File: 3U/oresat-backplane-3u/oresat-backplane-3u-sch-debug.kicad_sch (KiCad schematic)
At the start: 1 part, among them J1 m55-6001642

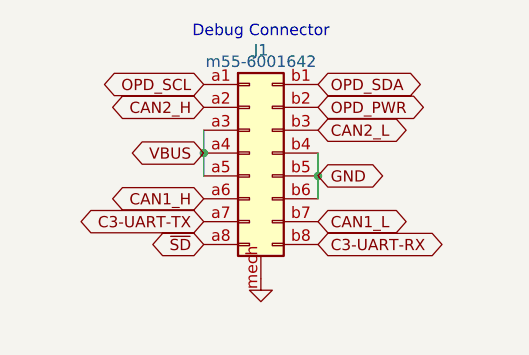
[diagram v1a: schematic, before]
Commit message: Can lines on back - need to move can resistors to front & add b.side solder mask
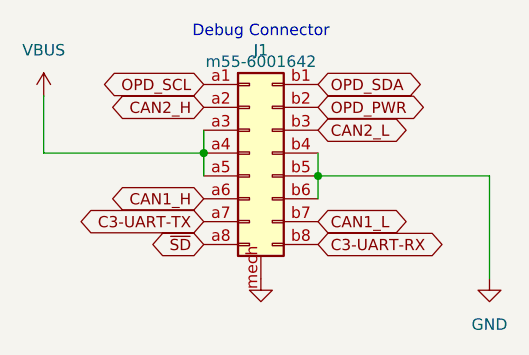
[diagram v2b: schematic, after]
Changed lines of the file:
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@@
+	(wire
+		(pts
+			(xy 167.64 114.3) (xy 167.64 120.65)
+		)
+		(stroke
+			(width 0)
+			(type default)
+		)
+	)
 	(wire
 		(pts
@@
 	(wire
 		(pts
+			(xy 217.17 123.19) (xy 198.12 123.19)
+		)
+		(stroke
+			(width 0)
+			(type default)
+		)
+	)
+	(wire
+		(pts
+			(xy 167.64 120.65) (xy 185.42 120.65)
+		)
+		(stroke
+			(width 0)
+			(type default)
+		)
+	)
+	(wire
+		(pts
 			(xy 198.12 120.65) (xy 198.12 123.19)
 		)
@@
 		)
 	)
+	(wire
+		(pts
+			(xy 217.17 134.62) (xy 217.17 123.19)
+		)
+		(stroke
+			(width 0)
+			(type default)
+		)
+	)
 	(global_label "OPD_SCL"
 		(shape bidirectional)
@@
 		)
 	)
-	(global_label "VBUS"
-		(shape bidirectional)
-		(at 185.42 120.65 180)
-		(fields_autoplaced yes)
-		(effects
-			(font
-				(size 1.2446 1.2446)
-			)
-			(justify right)
-		)
-		(property "Intersheetrefs" "${INTERSHEET_REFS}"
-			(at 233.68 288.29 0)
-			(effects
-				(font
-					(size 1.27 1.27)
-				)
-				(hide yes)
-			)
-		)
-	)
 	(global_label "OPD_PWR"
 		(shape bidirectional)
@@
 		(property "Intersheetrefs" "${INTERSHEET_REFS}"
 			(at 149.86 -31.75 0)
-			(effects
-				(font
-					(size 1.27 1.27)
-				)
-				(hide yes)
-			)
-		)
-	)
-	(global_label "GND"
-		(shape bidirectional)
-		(at 198.12 123.19 0)
-		(fields_autoplaced yes)
-		(effects
-			(font
-				(size 1.2446 1.2446)
-			)
-			(justify left)
-		)
-		(property "Intersheetrefs" "${INTERSHEET_REFS}"
-			(at 149.86 -59.69 0)
 			(effects
 				(font
@@
 					(unit 1)
 				)
+			)
+		)
+	)
+	(symbol
+		(lib_id "oresat-power:VBUS")
+		(at 167.64 114.3 0)
+		(unit 1)
+		(exclude_from_sim no)
+		(in_bom yes)
+		(on_board yes)
+		(dnp no)
+		(fields_autoplaced yes)
+		(property "Reference" "#VBUS031"
+			(at 167.64 118.11 0)
+			(effects
+				(font
+					(size 1.27 1.27)
+				)
+				(hide yes)
+			)
+		)
+		(property "Value" "VBUS"
+			(at 167.64 109.22 0)
+			(effects
+				(font
+					(size 1.27 1.27)
+				)
+			)
+		)
+		(property "Footprint" ""
+			(at 167.64 114.3 0)
+			(effects
+				(font
+					(size 1.27 1.27)
+				)
+				(hide yes)
+			)
+		)
+		(property "Datasheet" ""
+			(at 167.64 114.3 0)
+			(effects
+				(font
+					(size 1.27 1.27)
+				)
+				(hide yes)
+			)
+		)
+		(property "Description" "Power symbol creates a global label with name \"VBUS\""
+			(at 167.64 114.3 0)
+			(effects
+				(font
+					(size 1.27 1.27)
+				)
+				(hide yes)
+			)
+		)
+		(pin "1"
+		)
+		(instances
+			(project "oresat-backplane-3u"
+				(path "/300eeac4-6caf-4310-939c-5dc51539800c/0dfa61bf-7ec2-42f0-9843-5232fd59e79e"
+					(reference "#VBUS031")
+					(unit 1)
+				)
+			)
+		)
+	)
+	(symbol
+		(lib_id "power:GND")
+		(at 217.17 134.62 0)
+		(unit 1)
+		(exclude_from_sim no)
+		(in_bom yes)
+		(on_board yes)
+		(dnp no)
+		(fields_autoplaced yes)
+		(property "Reference" "#PWR029"
+			(at 217.17 140.97 0)
+			(effects
+				(font
+					(size 1.27 1.27)
+				)
+				(hide yes)
+			)
+		)
+		(property "Value" "GND"
+			(at 217.17 139.7 0)
+			(effects
+				(font
+					(size 1.27 1.27)
+				)
+			)
+		)
+		(property "Footprint" ""
+			(at 217.17 134.62 0)
+			(effects
+				(font
+					(size 1.27 1.27)
+				)
+				(hide yes)
+			)
+		)
+		(property "Datasheet" ""
+			(at 217.17 134.62 0)
+			(effects
+				(font
+					(size 1.27 1.27)
+				)
+				(hide yes)
+			)
+		)
+		(property "Description" "Power symbol creates a global label with name \"GND\" , ground"
+			(at 217.17 134.62 0)
+			(effects
+				(font
+					(size 1.27 1.27)
+				)
+				(hide yes)
+			)
+		)
+		(pin "1"
+		)
+		(instances
+			(project "oresat-backplane-3u"
+				(path "/300eeac4-6caf-4310-939c-5dc51539800c/0dfa61bf-7ec2-42f0-9843-5232fd59e79e"
+					(reference "#PWR029")
+					(unit 1)
+				)
